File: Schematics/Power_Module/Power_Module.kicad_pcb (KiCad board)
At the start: 4 copper layers, 69.5 x 60 mm, 131 parts, among them J1 ScrewSwitch, J2 Battery, J3 ScrewSwitch, J4 GSE, J5 USB_C_Female_USB2_Small, J6 SWD_B, J7 Stack Male Edge Connector, Q1 AO4447A, Q2 TSM2309CX, Q3 DMN6040SSD-13, SW1 SW_STM_RESET, SW2 SW_STM_BOOT_MODE, U1 TPS61175PWPR, U10 LM66100DCKR, U11 LM66100DCKR, U12 AMS1117-3.3, U13 CP2102N-A02-GQFN20R, U14 STM32F103CBT6, U15 ISO1044BDR, U16 W25Q128JVS, U2 LM74700QDBVRQ1, U3 LM74700QDBVRQ1, U4 ACS37041KLHBLT-010B3, U5 ACS37041KLHBLT-010B5, U6 INA181A2, U7 LMR51430XDDCR, U8 LMR51430XDDCR, U9 LM66100DCKR, Y1 X322516MMB4SI

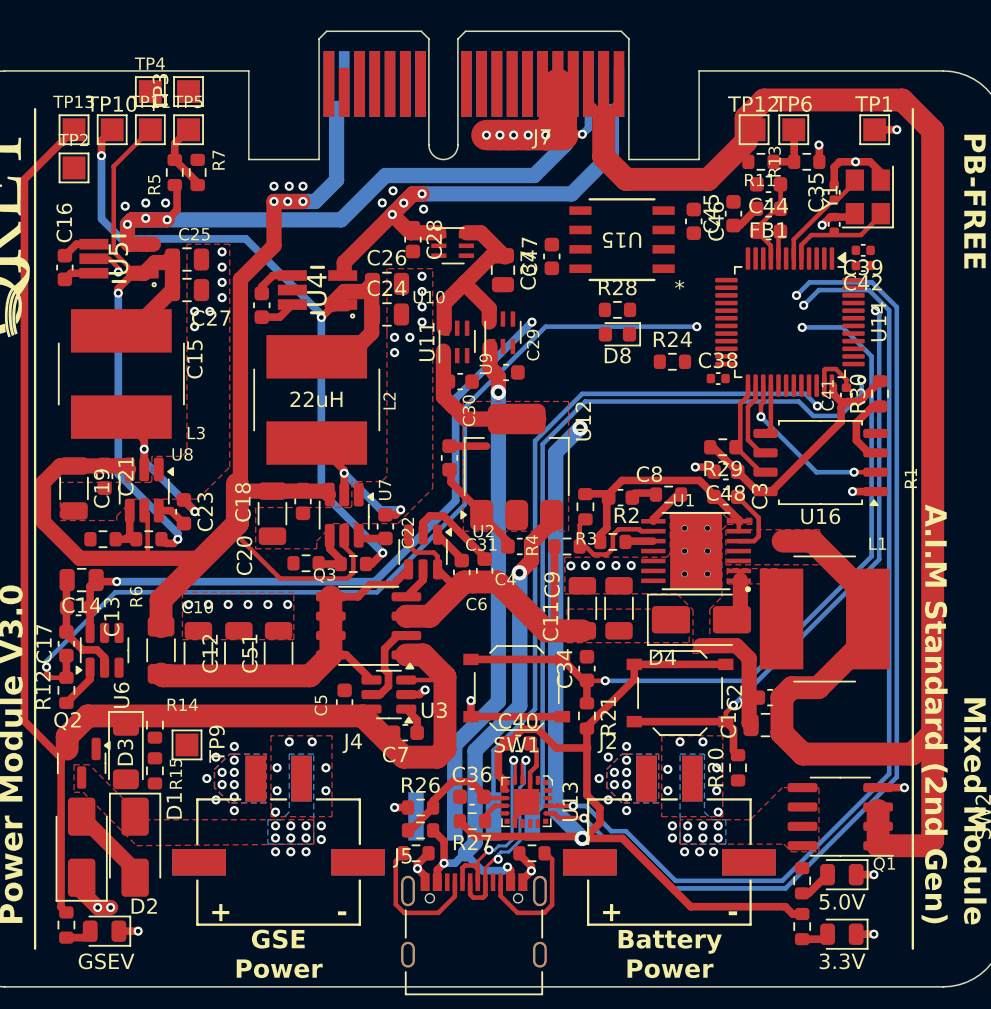
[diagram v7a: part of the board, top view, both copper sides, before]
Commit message: continuing to finish signal traces, added extra decouplping caps near PCIE
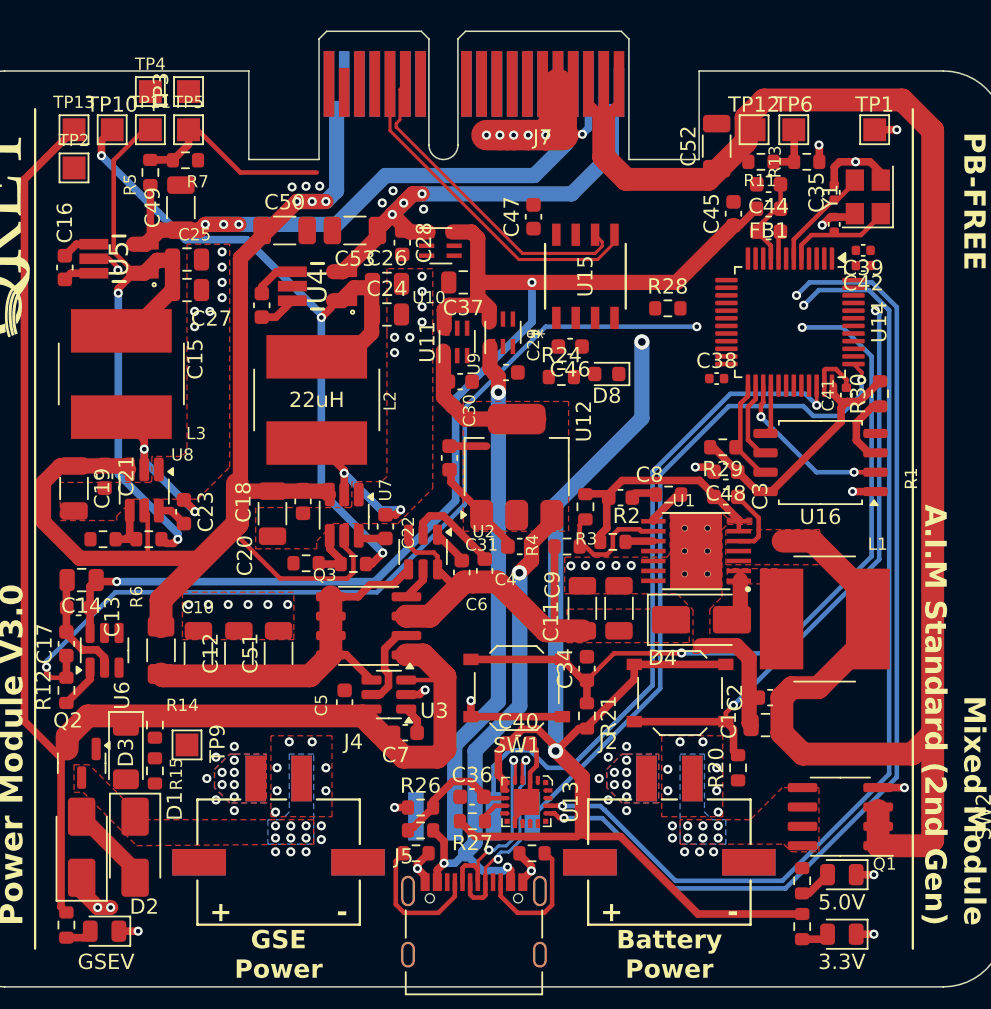
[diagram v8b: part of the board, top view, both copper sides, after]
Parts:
- added C49: 22uF, Capacitor_SMD:C_1206_3216Metric, F.Cu at (145.8, 48.7)
- added C50: 22uF, Capacitor_SMD:C_1206_3216Metric, F.Cu at (152.6, 50.2)
- added C52: 22uF, Capacitor_SMD:C_1206_3216Metric, F.Cu at (180.9, 44.7)
- added C53: 22uF, Capacitor_SMD:C_1206_3216Metric, F.Cu at (157.2, 50.2)
- moved C46 11.5 mm to (171.3, 57.8), turned to 0 degrees
- moved R24 7.34 mm to (170.7, 59.8)
- moved U15 3.39 mm to (172.3, 53.2), turned to 90 degrees
- moved R28 3.30 mm to (177.7, 55.3)
- moved C47 2.86 mm to (168.9, 49.3)
- moved C37 2.72 mm to (164.3, 53.6), turned to 180 degrees
- moved D8 2.69 mm to (173.7, 59.6)
- moved R5 1.60 mm to (143.8, 46.4)
- moved R7 1.13 mm to (146.1, 45.6), turned to 0 degrees
- moved U9 0.80 mm to (162.8, 51.2)
- moved C28 0.73 mm to (160.3, 51.0)
- moved U4 0.25 mm to (154.8, 53.9)
- moved C38 0.10 mm to (180.9, 59.9)
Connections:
- U1 pad 16: GND -> (no net)
- U1 pad 17: GND -> (no net)
- U1 pad 18: GND -> (no net)
- U1 pad 19: GND -> (no net)
- U1 pad 20: GND -> (no net)
- U1 pad 21: GND -> (no net)
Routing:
- net CAN_N: track 0.00 -> 22.2 mm
- net CAN_P: track 0.00 -> 21.1 mm
- net 3.3V_MUX: track 158.3 -> 177.8 mm
- net 5V_SENSE: track 4.62 -> 13.4 mm
- net SWCLK: track 48.6 -> 44.0 mm
- net 3.3V_PSU_Pre: track 53.7 -> 49.6 mm
- net 5V_PSU: track 46.7 -> 44.8 mm
- net SWDIO: track 45.8 -> 45.3 mm
- net GND: track 127.2 -> 127.3 mm, vias 91 -> 88
